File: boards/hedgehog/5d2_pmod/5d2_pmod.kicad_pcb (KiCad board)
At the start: 2 copper layers, 100 x 100 mm, 23 parts

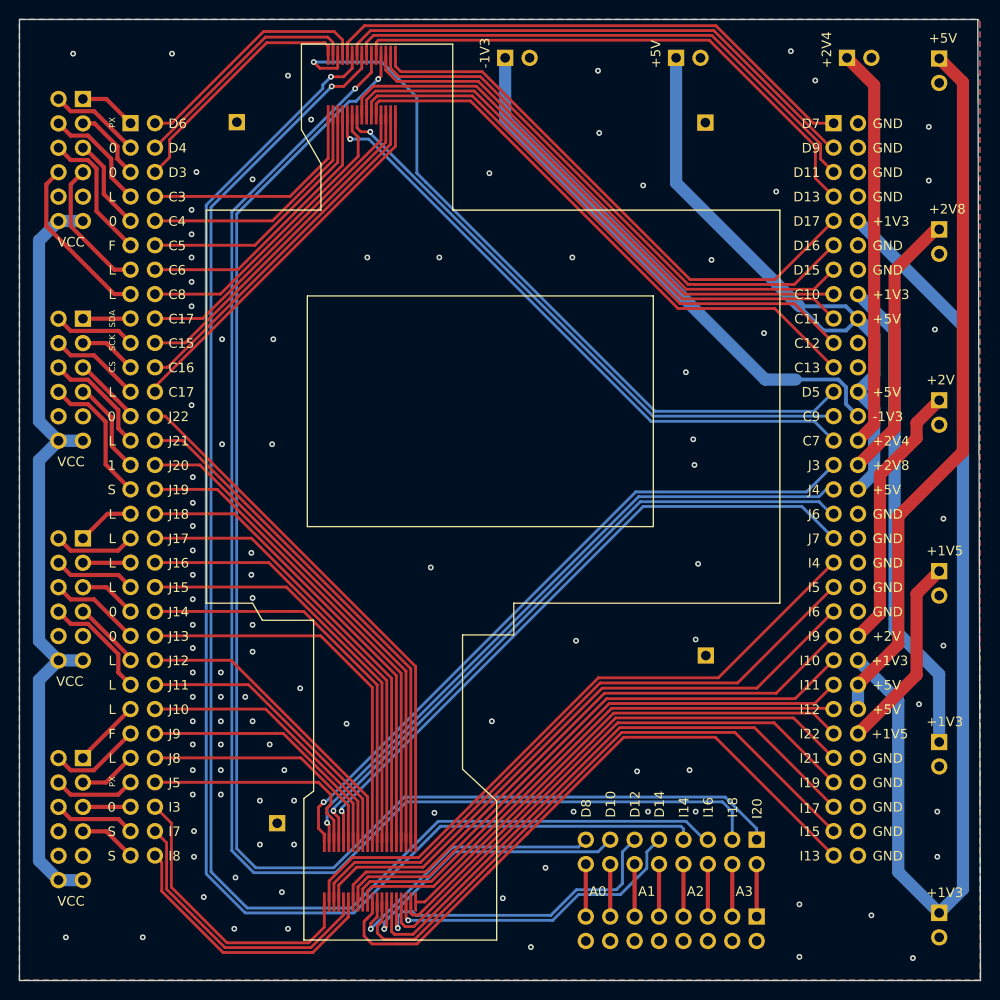
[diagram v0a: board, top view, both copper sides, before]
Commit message: secend revision of hedgehog/5d2_pmod board
the first revision sadly had wrong row spacing for the sensor connectors and was thus unusable
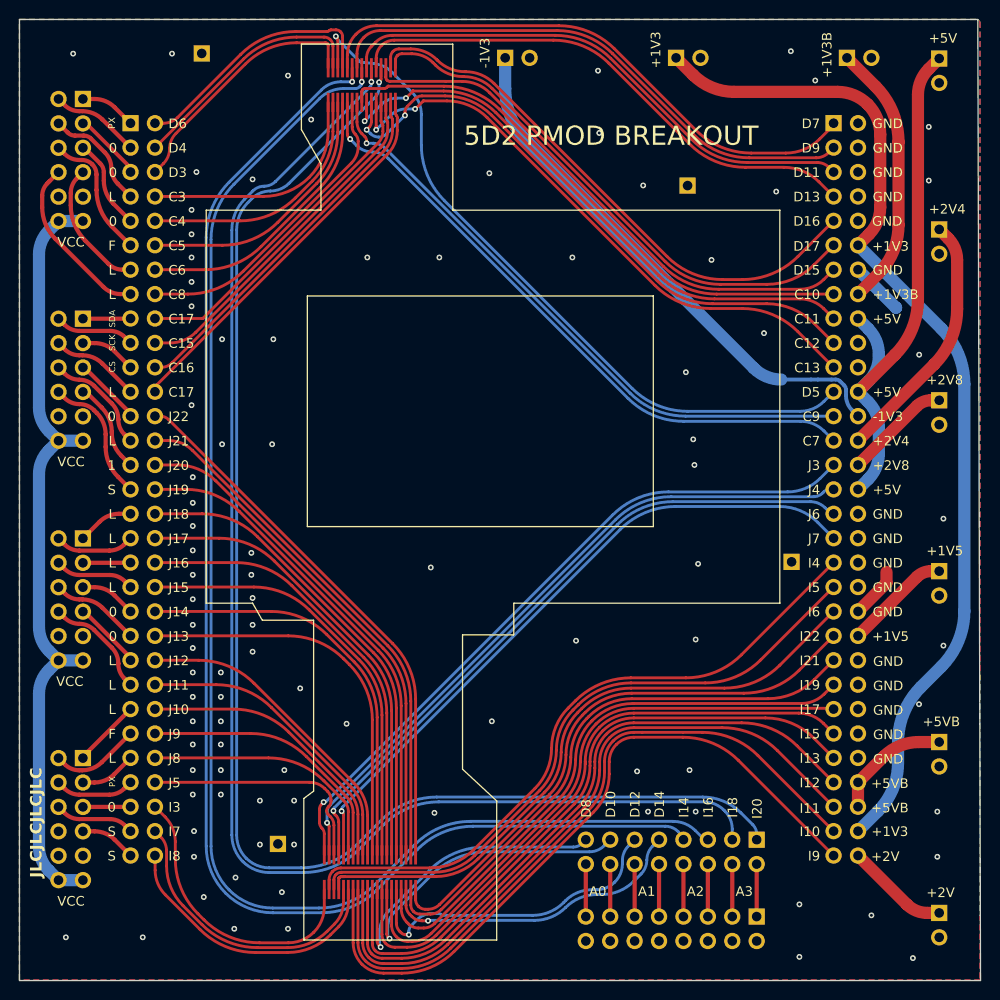
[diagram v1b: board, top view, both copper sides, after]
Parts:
- added G***: LOGO, 2d5:no_camera_is_a_kodak, F.Cu at (178.1, 136.0)
- added G***: LOGO, 2d5:camera, B.Cu at (162.8, 107.5)
- moved PWR1 71.1 mm to (209.0, 68.6)
- moved PWR6 53.3 mm to (209.0, 121.9)
- moved PWR5 53.3 mm to (209.0, 157.5)
- moved PWR2 17.8 mm to (209.0, 139.7)
- moved PWR4 17.8 mm to (209.0, 104.1)
- moved GND2 13.2 mm to (193.6, 121.0)
- moved GND0 8.03 mm to (132.2, 68.0)
- moved GND3 6.81 mm to (182.8, 81.8)
- moved GND1 2.15 mm to (140.2, 150.3)
- renumbered PWR7 to PWR1, PWR8 to PWR2, PWR4 to PWR3, PWR6 to PWR4, PWR2 to PWR6, PWR3 to PWR7, PWR1 to PWR8
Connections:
- JP1 pad 10: +1V3 -> GND
- JP1 pad 11: /GND_5 -> /+1V3_TOP
- JP1 pad 12: GND -> +1V3
- JP1 pad 43: /+2V_0 -> /+1V5_0
- JP1 pad 44: +2V -> +1V5
- JP1 pad 45: /+1V3_BOT -> /GND_8
- JP1 pad 46: +1V3 -> GND
- JP1 pad 47: /+5Vb_1 -> /GND_9
- JP1 pad 48: +5VB -> GND
- JP1 pad 49: /+5Vb_0 -> /GND_10
- JP1 pad 50: +5VB -> GND
- JP1 pad 51: /+1V5_0 -> /GND_11
- JP1 pad 52: +1V5 -> GND
- JP1 pad 53: /GND_8 -> /GND_12
- JP1 pad 55: /GND_9 -> /+5Vb_0
- JP1 pad 56: GND -> +5VB
- JP1 pad 57: /GND_10 -> /+5Vb_1
- JP1 pad 58: GND -> +5VB
- JP1 pad 59: /GND_11 -> /+1V3_BOT
- JP1 pad 60: GND -> +1V3
- JP1 pad 61: /GND_12 -> /+2V_0
- JP1 pad 62: GND -> +2V
- JP1 pad 9: /+1V3_TOP -> /GND_5
- PWR1 pad 1: +1V3B -> +5V
- PWR2 pad 1: +1V3 -> +5VB
- PWR3 pad 1: +2V8 -> +2V4
- PWR4 pad 1: +1V5 -> +2V8
- PWR6 pad 1: +5VB -> +1V5
- PWR7 pad 1: +2V4 -> +1V3B
- PWR8 pad 1: +5V -> +1V3
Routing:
- net +5VB: track 73.2 -> 12.5 mm
- net +1V3B: track 50.1 -> 27.8 mm
- net +2V: track 28.0 -> 10.8 mm
- net +2V8: track 28.2 -> 11.1 mm
- net +2V4: track 41.7 -> 26.5 mm
- net /+5Vb_1: track 59.2 -> 70.7 mm
- net /+1V3_BOT: track 60.8 -> 72.4 mm
- net /+2V_0: track 62.5 -> 74.0 mm
- net /+5Vb_0: track 57.6 -> 69.1 mm
- net GND: track 0.00 -> 10.9 mm, vias 101 -> 94
- net +1V5: track 20.4 -> 11.1 mm
- net +5V: track 67.3 -> 58.3 mm
- net /+1V5_0: track 52.5 -> 58.4 mm
- net A1-: track 29.3 -> 33.3 mm
- net A3-: track 148.6 -> 145.0 mm
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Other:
- board text added: "+1V3B"
- board text added: "+5VB"
- board text added: "5D2 PMOD BREAKOUT"
- board text added: "JLCJLCJLCJLC"
